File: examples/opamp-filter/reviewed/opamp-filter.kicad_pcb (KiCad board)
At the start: 2 copper layers, 58 x 42 mm, 22 parts, among them J1 IN, J2 5V, J3 OUT, U1 MCP6001R, U2 MCP6001R

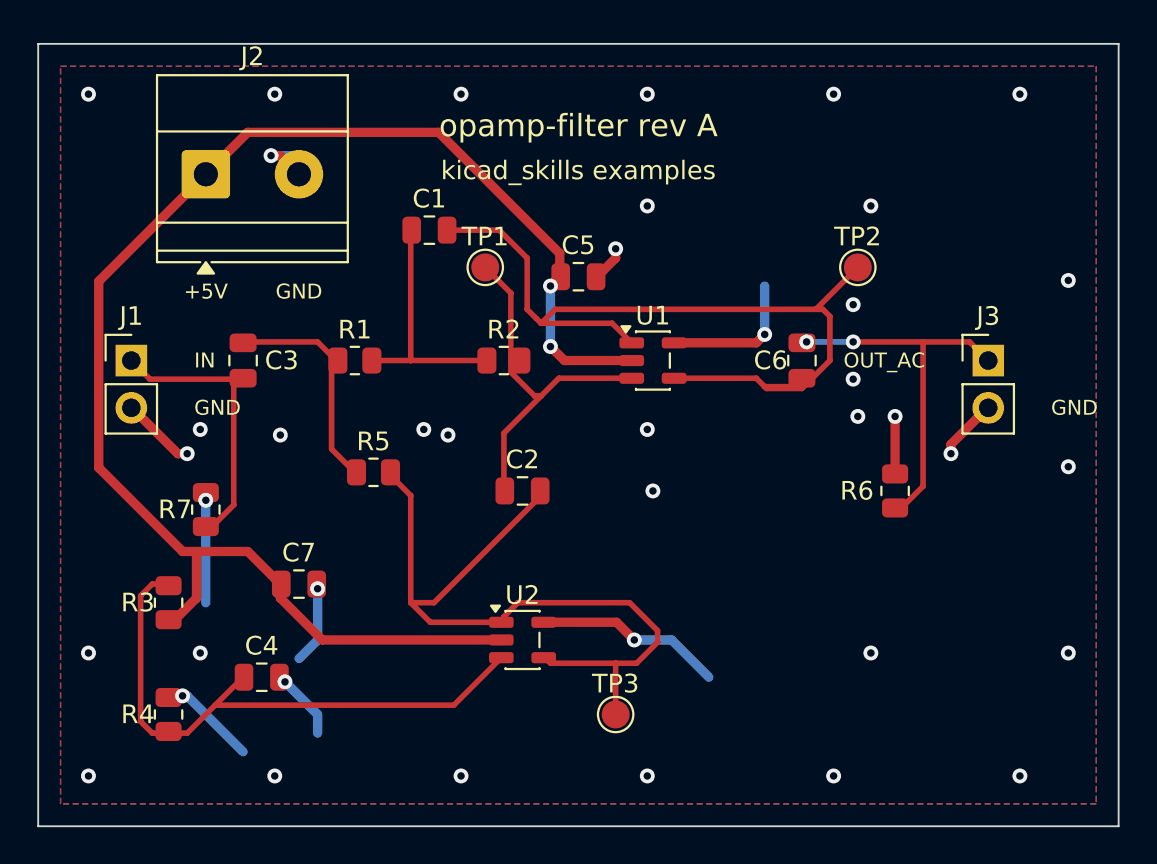
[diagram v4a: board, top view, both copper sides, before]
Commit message: Keep vias out of the lands they would drain
The reviewer's next one, and it is not one board's problem: vias were
landing inside surface-mount lands across the set. A hole in a land is a
hole solder wicks down during reflow - the joint above it starves, and
nothing on the assembled board tells that apart from a cold one.
Via-in-pad is a real technique and a filled-and-capped process, not a
drawing; a layout that has not specified the process may not draw it.

The router was the source. `_blocked` skips a route's own net, so
nothing stopped a layer change from happening on the very land the route
started at, and eighteen vias across three boards sat in one. Pads are
now marked as pads in the obstacle list and every one of them, whoever
owns it, is a cell where a via may not go - so an escape that has to
reach the plane leaves the land first and turns its via beside it. The
stitching pass kept ground vias a via-radius from ground lands where it
kept signal ones a radius plus clearance; both are the same distance
now, because the plane gains nothing from touching a land it can reach a
stub away.

`via.in_pad` measures the copper gap from every via to every land and
reports what is left. The exposed thermal pad under a package is exempt
- the via array in one is the datasheet's own answer, and nothing a
signal reaches is four square millimetres. It blocks under the
ai-generated policy: a generated board has no reason to draw this.

The test fixture had one too, a via twenty-five microns into C1's ground
land; it moves three tenths of a millimetre and the board is DRC clean
on both matrix versions as before.

Co-Authored-By: Claude Fable 5 <noreply@anthropic.com>
Claude-Session: https://claude.ai/code/session_01DUj7Ltu92tWg159mCSacwY
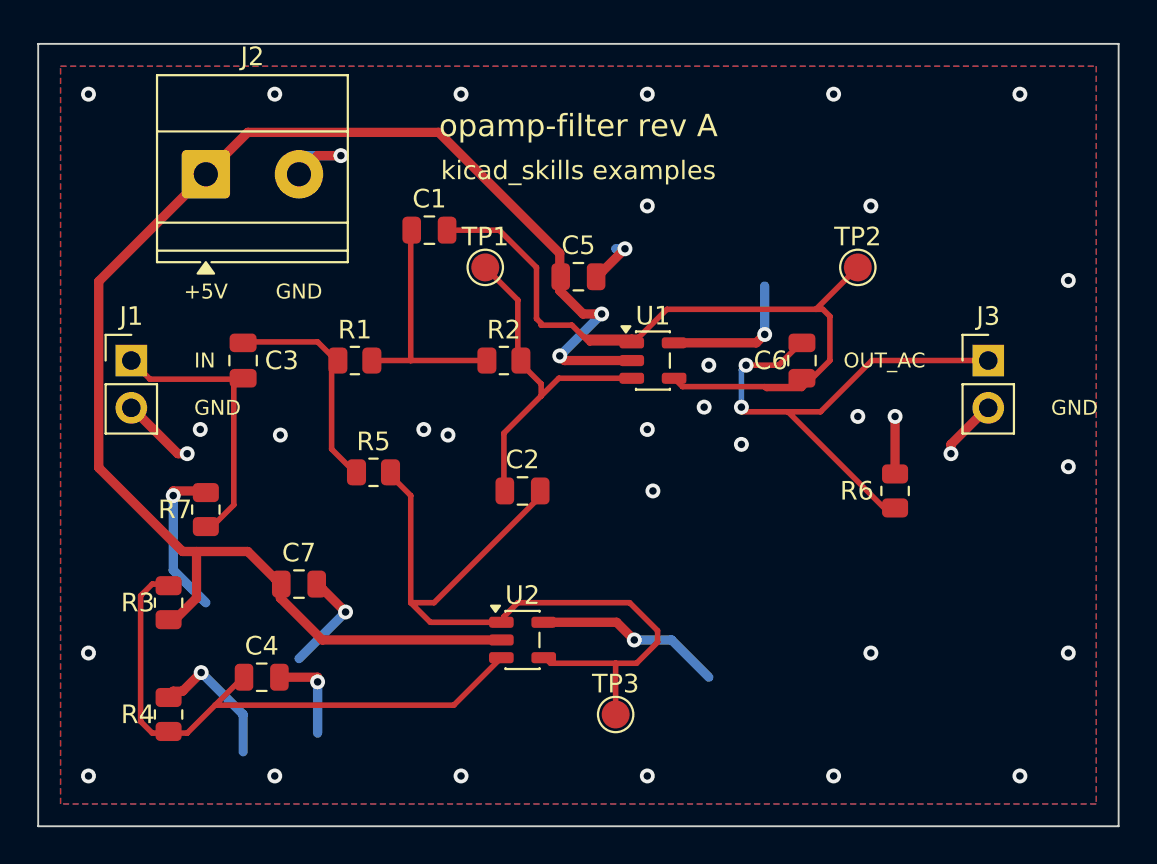
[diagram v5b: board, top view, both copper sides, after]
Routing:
- net GND: track 53.0 -> 62.5 mm
- net /OUT_AC: track 20.2 -> 28.5 mm
- net +5V: track 81.2 -> 83.2 mm
- net /OUT: track 47.0 -> 45.0 mm
- net /FILT_IN: track 20.4 -> 19.3 mm

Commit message: Give the vias room to stand beside the lands
Following the via-in-pad ban, the FPGA board stopped routing: five
attempts, five different nets, each one out of lanes in the corridor
between the FPGA's east escape fan and the codec's west one. Three
changes, in the order a layout would make them.

The via spacing was guesswork and is now the fab's. Hole to hole goes
from 1.2 mm to 0.9, which at the shipped 0.8/0.4 via leaves half a
millimetre of laminate between barrels - the ordinary minimum - and in a
1 mm-pitch escape comb is the difference between a lane and no lane.
What a via keeps off a land it may not sit in is its own radius plus a
solder-mask dam rather than the track clearance: the copper either side
may well be the same net, and what has to be true is that the mask can
part the barrel from the land.

Every decoupling capacitor now has its ground via placed against its own
pad rather than nine of them asking the search for one, and where the
via goes is chosen rather than fixed: `anchor_site` takes the nearest
position that clears everything already placed, fanning either side of
the direction facing off the part. A fixed offset walled off the
corridor its neighbour's supply needed - the via was legal, and it was
in the way.

And the seven parts sitting inside that corridor - four decoupling
capacitors, the two 1.2 V ones and the LED resistor - move four
millimetres south into the empty band below it. Twelve lanes leaving the
FPGA and ten arriving at the codec have eleven millimetres to cross in;
what a hand would do first is stop parking capacitors in the middle of
that, and it is the floorplan half of the debt this board's own README
has been carrying.

Co-Authored-By: Claude Fable 5 <noreply@anthropic.com>
Claude-Session: https://claude.ai/code/session_01DUj7Ltu92tWg159mCSacwY
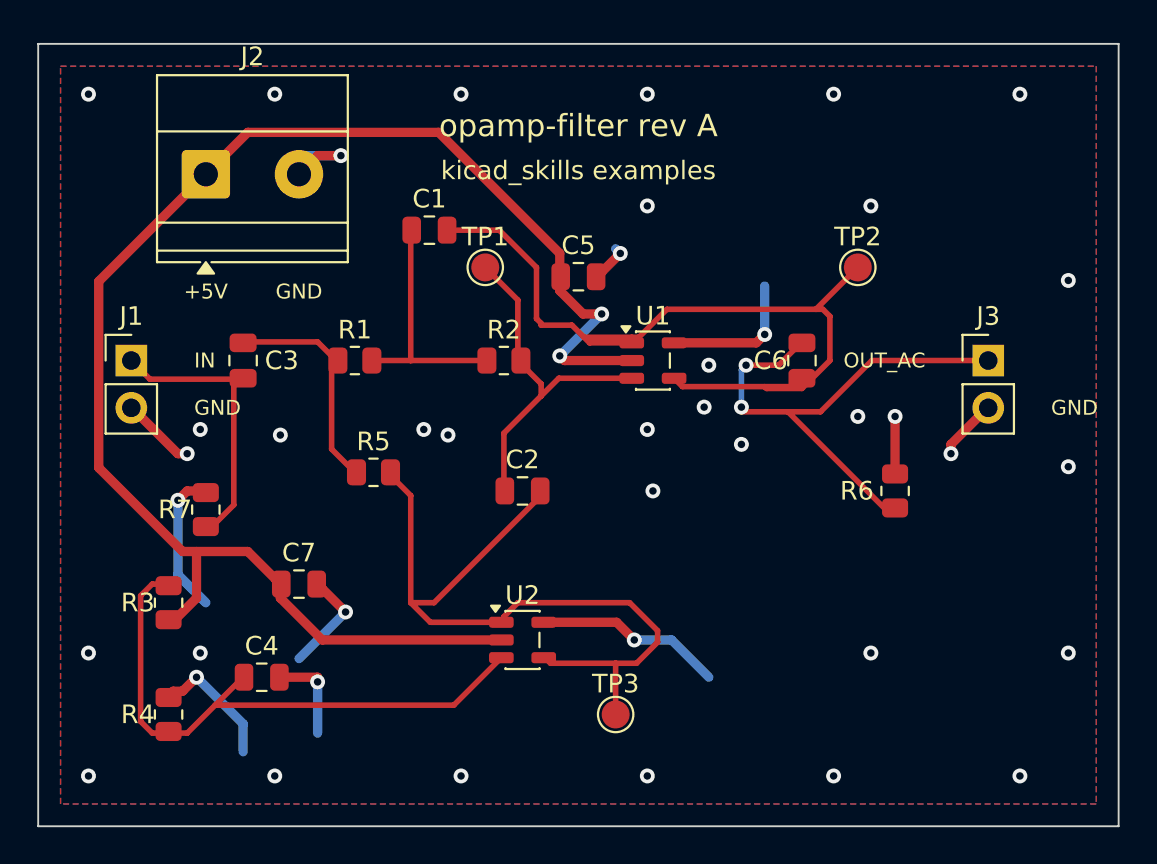
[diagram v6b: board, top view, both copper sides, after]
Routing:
- net GND: track 62.5 -> 60.9 mm, vias 40 -> 41
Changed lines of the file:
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@@
 	(segment (start 109.0 84.0875) (end 108.8375 84.0875) (width 0.5) (layer "F.Cu") (net 1))
 	(segment (start 108.8375 84.0875) (end 108.75 84.0) (width 0.5) (layer "F.Cu") (net 1))
-	(segment (start 108.75 84.0) (end 107.25 84.0) (width 0.5) (layer "F.Cu") (net 1))
-	(segment (start 107.25 84.0) (end 107.25 84.25) (width 0.5) (layer "F.Cu") (net 1))
-	(segment (start 107.25 84.25) (end 107.25 88.25) (width 0.5) (layer "B.Cu") (net 1))
-	(segment (start 107.25 88.25) (end 109.0 90.0) (width 0.5) (layer "B.Cu") (net 1))
+	(segment (start 108.75 84.0) (end 108.0 84.0) (width 0.5) (layer "F.Cu") (net 1))
+	(segment (start 108.0 84.0) (end 107.5 84.5) (width 0.5) (layer "F.Cu") (net 1))
+	(segment (start 107.5 84.5) (end 107.5 88.5) (width 0.5) (layer "B.Cu") (net 1))
+	(segment (start 107.5 88.5) (end 109.0 90.0) (width 0.5) (layer "B.Cu") (net 1))
 	(segment (start 114.0 67.0) (end 115.0 66.0) (width 0.5) (layer "F.Cu") (net 1))
 	(segment (start 115.0 66.0) (end 116.25 66.0) (width 0.5) (layer "F.Cu") (net 1))
@@
 	(segment (start 129.95 72.5) (end 130.0 72.5) (width 0.5) (layer "F.Cu") (net 1))
 	(segment (start 130.0 72.5) (end 130.25 72.25) (width 0.5) (layer "F.Cu") (net 1))
-	(segment (start 130.25 72.25) (end 131.5 71.0) (width 0.5) (layer "F.Cu") (net 1))
-	(segment (start 131.5 71.0) (end 131.0 71.0) (width 0.5) (layer "B.Cu") (net 1))
+	(segment (start 130.25 72.25) (end 131.25 71.25) (width 0.5) (layer "F.Cu") (net 1))
+	(segment (start 131.25 71.25) (end 131.0 71.0) (width 0.5) (layer "B.Cu") (net 1))
 	(segment (start 114.95 89.0) (end 115.0 89.0) (width 0.5) (layer "F.Cu") (net 1))
 	(segment (start 115.0 89.0) (end 115.25 89.25) (width 0.5) (layer "F.Cu") (net 1))
@@
 	(segment (start 107.0 95.0) (end 107.25 94.75) (width 0.5) (layer "F.Cu") (net 1))
 	(segment (start 107.25 94.75) (end 107.75 94.75) (width 0.5) (layer "F.Cu") (net 1))
-	(segment (start 107.75 94.75) (end 108.75 93.75) (width 0.5) (layer "F.Cu") (net 1))
-	(segment (start 108.75 93.75) (end 111.0 96.0) (width 0.5) (layer "B.Cu") (net 1))
-	(segment (start 111.0 96.0) (end 111.0 98.0) (width 0.5) (layer "B.Cu") (net 1))
+	(segment (start 107.75 94.75) (end 108.5 94.0) (width 0.5) (layer "F.Cu") (net 1))
+	(segment (start 108.5 94.0) (end 111.0 96.5) (width 0.5) (layer "B.Cu") (net 1))
+	(segment (start 111.0 96.5) (end 111.0 98.0) (width 0.5) (layer "B.Cu") (net 1))
 	(segment (start 139.0 75.6) (end 139.0 73.0) (width 0.5) (layer "B.Cu") (net 1))
 	(segment (start 132.0 92.0) (end 134.0 92.0) (width 0.5) (layer "B.Cu") (net 1))
@@
 	(via (at 133.0 84.0) (size 0.8) (drill 0.4) (layers "F.Cu" "B.Cu") (net 1))
 	(via (at 144.0 80.0) (size 0.8) (drill 0.4) (layers "F.Cu" "B.Cu") (net 1))
-	(via (at 131.5 71.0) (size 0.8) (drill 0.4) (layers "F.Cu" "B.Cu") (net 1))
+	(via (at 131.25 71.25) (size 0.8) (drill 0.4) (layers "F.Cu" "B.Cu") (net 1))
 	(via (at 130.25 74.5) (size 0.8) (drill 0.4) (layers "F.Cu" "B.Cu") (net 2))
 	(via (at 128.0 76.75) (size 0.8) (drill 0.4) (layers "F.Cu" "B.Cu") (net 2))
@@
 	(via (at 149.0 82.0) (size 0.8) (drill 0.4) (layers "F.Cu" "B.Cu") (net 1))
 	(via (at 146.0 80.0) (size 0.8) (drill 0.4) (layers "F.Cu" "B.Cu") (net 1))
-	(via (at 107.25 84.25) (size 0.8) (drill 0.4) (layers "F.Cu" "B.Cu") (net 1))
+	(via (at 107.5 84.5) (size 0.8) (drill 0.4) (layers "F.Cu" "B.Cu") (net 1))
 	(via (at 116.25 66.0) (size 0.8) (drill 0.4) (layers "F.Cu" "B.Cu") (net 1))
 	(via (at 116.5 90.5) (size 0.8) (drill 0.4) (layers "F.Cu" "B.Cu") (net 1))
 	(via (at 115.0 94.25) (size 0.8) (drill 0.4) (layers "F.Cu" "B.Cu") (net 1))
-	(via (at 108.75 93.75) (size 0.8) (drill 0.4) (layers "F.Cu" "B.Cu") (net 1))
+	(via (at 108.5 94.0) (size 0.8) (drill 0.4) (layers "F.Cu" "B.Cu") (net 1))
 	(via (at 132.0 92.0) (size 0.8) (drill 0.4) (layers "F.Cu" "B.Cu") (net 1))
 	(via (at 139.0 75.6) (size 0.8) (drill 0.4) (layers "F.Cu" "B.Cu") (net 1))
@@
 	(via (at 120.7 80.7) (size 0.8) (drill 0.4) (layers "F.Cu" "B.Cu") (net 1))
 	(via (at 132.7 80.7) (size 0.8) (drill 0.4) (layers "F.Cu" "B.Cu") (net 1))
+	(via (at 108.7 92.7) (size 0.8) (drill 0.4) (layers "F.Cu" "B.Cu") (net 1))
 	(via (at 144.7 92.7) (size 0.8) (drill 0.4) (layers "F.Cu" "B.Cu") (net 1))
 	(zone

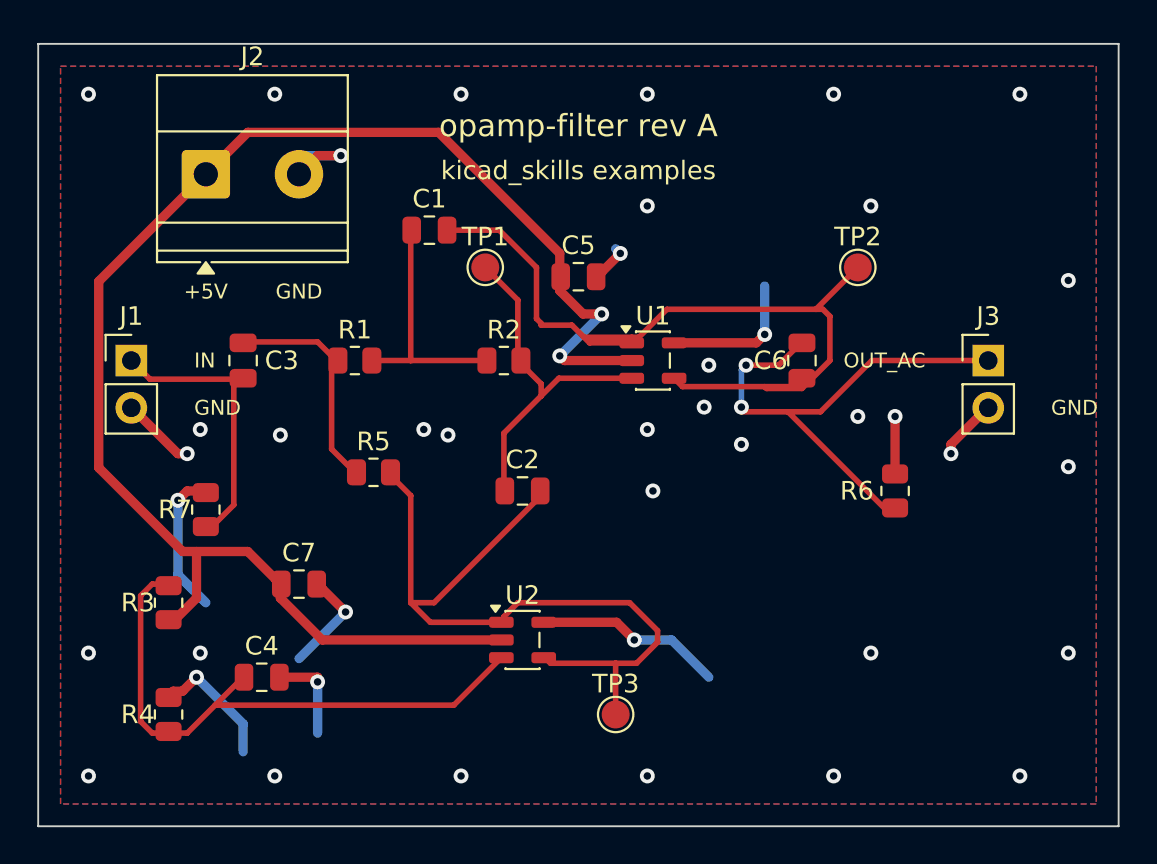
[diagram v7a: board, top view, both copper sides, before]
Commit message: Relieve the pads, fillet the joints, and give the board its screw holes
Three of the reviewer's manufacturing points, and they largely fall out
of the one before it - once KiCad fills the plane, the thermal relief it
was already asked for in the file actually appears.

**Thermal relief.** The zones said thermal all along; our own filler
ignored it and flooded every land solid. KiCad's does not, so every
through-hole ground pad now sits in a gap bridged by four spokes and an
iron can bring the joint up without heating a hundred square millimetres
of copper. `layout.solid_pad_connection` reports the setting when a
board turns it off: drilled pads only, because a surface pad reflows in
an oven that is heating the plane anyway and flooding it is often the
better thermal answer.

**Teardrops.** A track entering a land is a step change in width, and a
step change is where copper tears - the connector gets levered on and
off, the drill wanders, and the crack starts at the corner. `_teardrops`
replaces the first stretch of each run with a three-step taper into the
land, checked against its neighbours before it is kept, so a fillet
never eats the clearance a fine-pitch escape needs. It *replaces* rather
than overlays: laying the taper on top of the run drew the same copper
twice, and `route.acute_angle` reported all thirty of them, correctly.
`route.mixed_track_widths` learns what a fillet looks like so a properly
filleted board does not read as one nobody decided the width of.

**Mounting holes.** Four M3 holes near the corners, placed before the
router runs because they are obstacles, and slid along the edges or a
little inboard where a connector body has the corner - the motor board
and the op-amp take three, which is what those floorplans have room for.
Grounded on the motor driver, whose chassis is metal and part of the
shield, plain on the rest: bonding the enclosure to the reference is the
enclosure's decision, not the board's.

Two things that fell out of placing par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
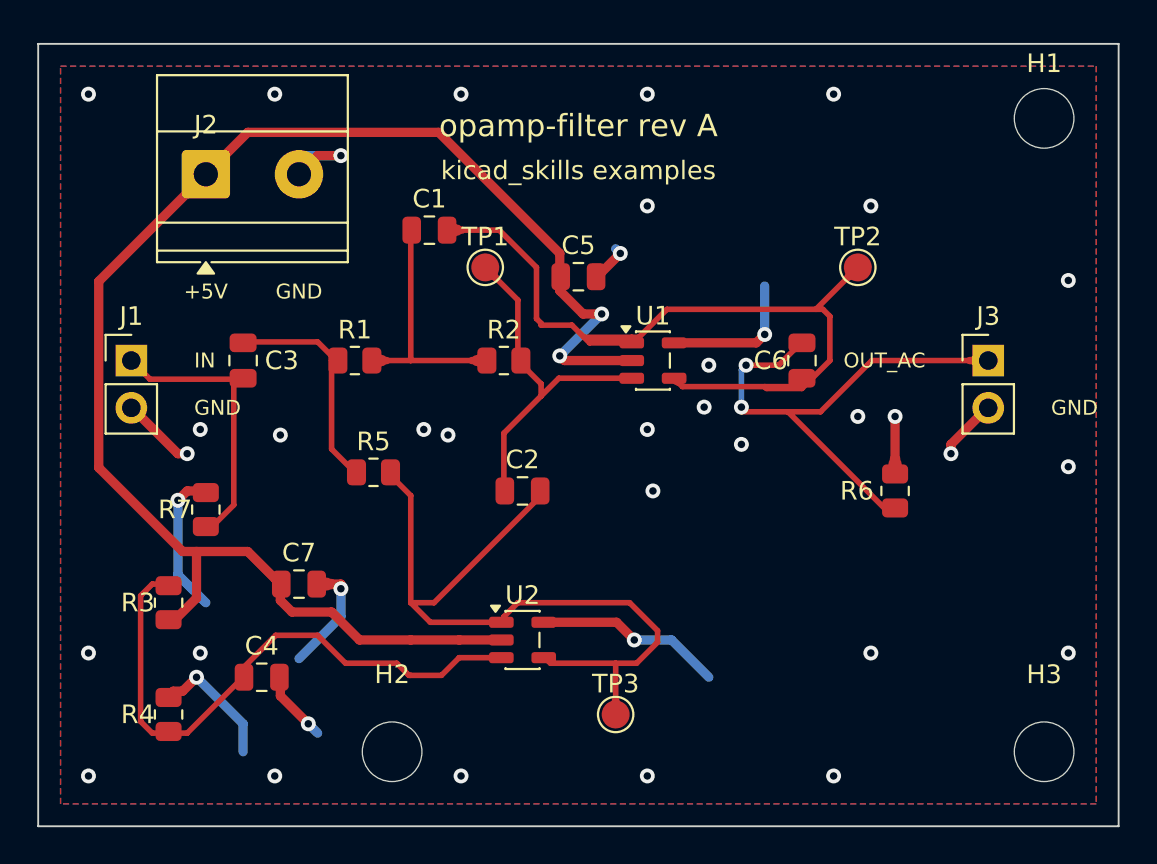
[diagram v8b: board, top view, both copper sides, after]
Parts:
- added H1: M33, MountingHole:MountingHole_3.2mm_M3, F.Cu at (154.0, 64.0)
- added H2: M33, MountingHole:MountingHole_3.2mm_M3, F.Cu at (119.0, 98.0)
- added H3: M33, MountingHole:MountingHole_3.2mm_M3, F.Cu at (154.0, 98.0)
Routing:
- net GND: track 60.9 -> 60.2 mm, vias 41 -> 39
